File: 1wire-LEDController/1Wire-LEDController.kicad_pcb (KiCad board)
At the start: 2 copper layers, 99.8 x 99.8 mm, 33 parts, among them CON1 BARREL_JACK, J1 RJ45, J2 RJ45, P1 SWD, P2 Power Enable, P3 CONN_01X05, P4 DC_IN, P5 CONN_01X05, P6 UART, Q1 IRLZ44NS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

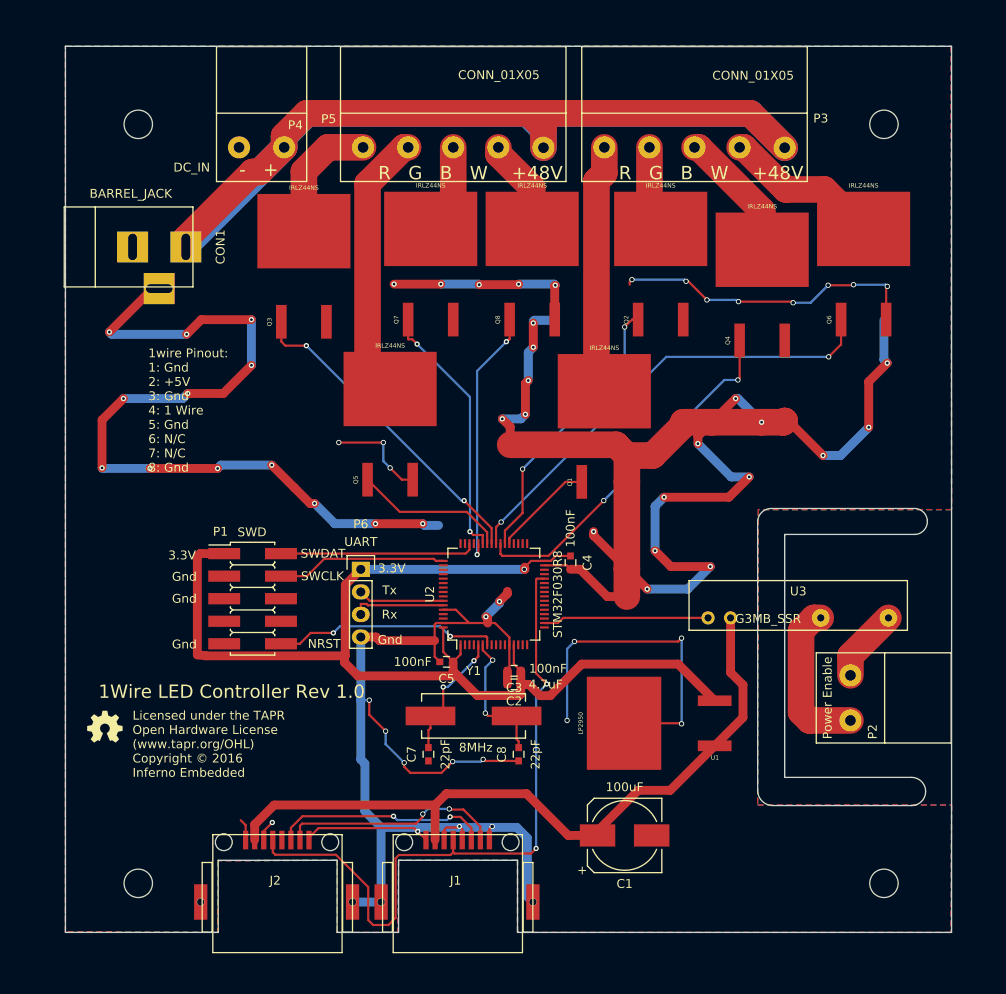
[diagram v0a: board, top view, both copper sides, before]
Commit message: Add 4 channel RGBW LED controller
Signed-off-by: Alastair D'Silva <alastair@d-silva.org>
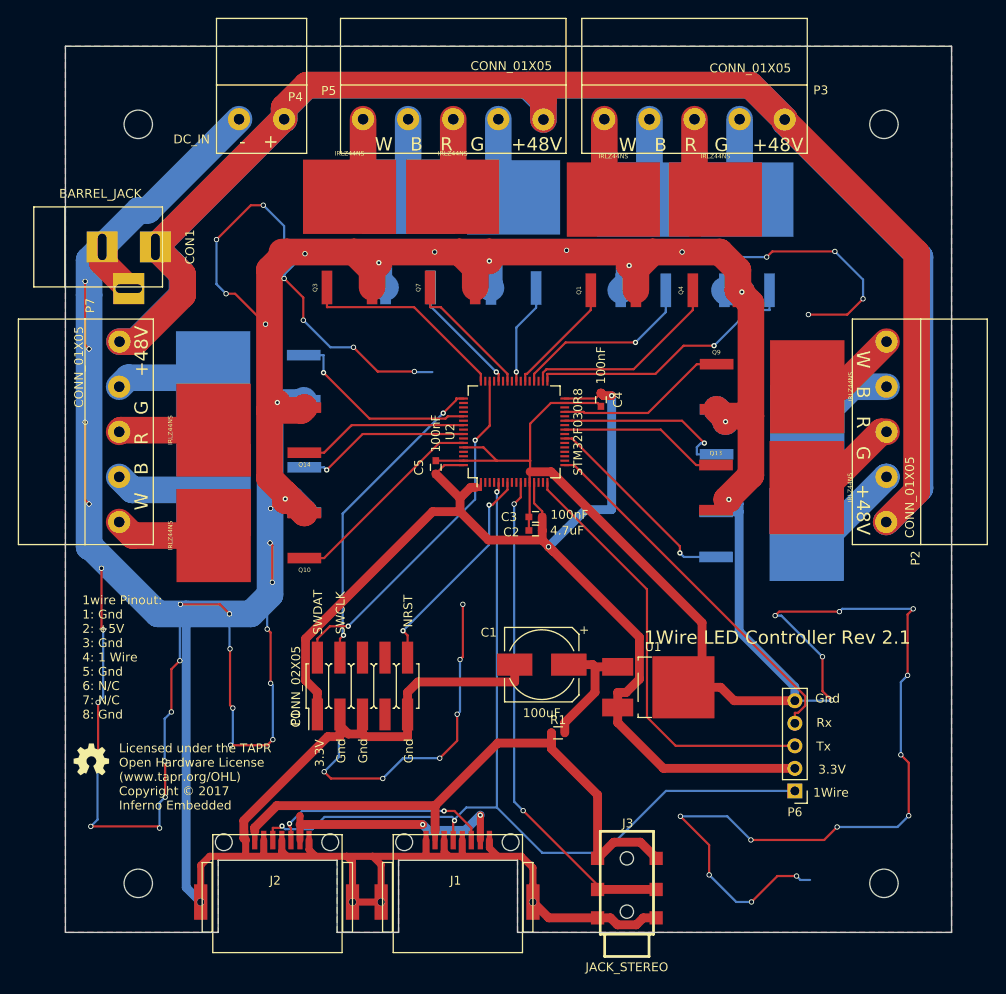
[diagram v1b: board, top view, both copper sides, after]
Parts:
- removed C7, C8: 22pF, Capacitors_SMD:C_0603
- removed U3: G3MB_SSR, SSR:G3MB
- removed Y1: 8MHz, Crystals:Crystal_HC49-SD_SMD
- added J3: JACK_STEREO, w_conn_av:jack_3.5_pj313d-smt, F.Cu at (193.0, 154.9)
- added P7: CONN_01X05, 2EDCK-Screw-Connectors:2EDCK-5.08-5PIN, F.Cu at (139.7, 116.8)
- added Q10: IRLZ44NS, kicad-open-modules:D2PAK, F.Cu at (146.5, 115.8)
- added Q11: IRLZ44NS, kicad-open-modules:D2PAK, B.Cu at (213.4, 104.1)
- added Q12: IRLZ44NS, kicad-open-modules:D2PAK, B.Cu at (146.5, 110.7)
- added Q13: IRLZ44NS, kicad-open-modules:D2PAK, F.Cu at (213.3, 110.4)
- added Q14: IRLZ44NS, kicad-open-modules:D2PAK, F.Cu at (146.5, 104.0)
- added Q15: IRLZ44NS, kicad-open-modules:D2PAK, B.Cu at (213.3, 115.7)
- added Q16: IRLZ44NS, kicad-open-modules:D2PAK, B.Cu at (146.4, 98.0)
- added Q9: IRLZ44NS, kicad-open-modules:D2PAK, F.Cu at (213.4, 99.1)
- added R1: 33R, Resistors_SMD:R_0603, F.Cu at (185.3, 138.0)
- P1: value SWD -> CONN_02X05
- P2: value Power Enable -> CONN_01X05; footprint 2EDCK-Screw-Connectors:2EDCK-5.08-2PIN -> 2EDCK-Screw-Connectors:2EDCK-5.08-5PIN
- P6: value UART -> CONN_01X05; footprint Pin_Headers:Pin_Header_Straight_1x04 -> Pin_Headers:Pin_Header_Straight_1x05_Pitch2.54mm
- Q2, Q5, Q6, Q8: moved to B.Cu
- U1: footprint kicad-open-modules:D2PAK -> TO_SOT_Packages_SMD:TO-252-2Lead
- moved P6 54.9 mm to (212.0, 144.6), turned to 180 degrees
- moved P2 37.8 mm to (218.4, 91.4)
- moved C5 21.9 mm to (171.5, 108.1), turned to 90 degrees
- moved Q5 21.7 mm to (168.4, 77.7), turned to 180 degrees
- moved Q1 21.6 mm to (191.5, 78.0)
- moved C1 21.4 mm to (183.5, 130.4), turned to 180 degrees
- moved C4 18.7 mm to (190.1, 100.5)
- moved U2 18.4 mm to (180.3, 104.1)
- moved C2 17.5 mm to (182.8, 115.3)
- moved C3 17.5 mm to (182.8, 113.7)
- moved P1 15.8 mm to (163.3, 132.8), turned to 0 degrees
- moved Q6 13.6 mm to (206.6, 78.0), turned to 180 degrees
- moved Q4 7.73 mm to (203.0, 78.0)
- moved Q3 6.44 mm to (161.8, 77.7)
- moved U1 5.04 mm to (195.7, 132.9), turned to 0 degrees
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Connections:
- net /PWM_Driver/SWCLK renamed /SWCLK
- net /PWM_Driver/SWDAT renamed /SWDAT
- C1 pad 1: +5V -> Net-(C1-Pad1)
- P6 pad 1: +3V3 -> /1W-DATA
- P6 pad 2: Net-(P6-Pad2) -> +3V3
- P6 pad 3: Net-(P6-Pad3) -> /UART_TX
- P6 pad 4: GND -> /UART_RX
- Q1 pad 1: Net-(Q1-Pad1) -> /CHAN2_R
- Q2 pad 1: Net-(Q2-Pad1) -> /CHAN2_G
- Q3 pad 1: Net-(Q3-Pad1) -> /CHAN1_R
- Q4 pad 1: Net-(Q4-Pad1) -> /CHAN2_B
- Q5 pad 1: Net-(Q5-Pad1) -> /CHAN1_G
- Q6 pad 1: Net-(Q6-Pad1) -> /CHAN2_W
- Q7 pad 1: Net-(Q7-Pad1) -> /CHAN1_B
- Q8 pad 1: Net-(Q8-Pad1) -> /CHAN1_W
- U1 pad 1: +5V -> Net-(C1-Pad1)
- U2 pad 10: (no net) -> /MAINS_ENABLE
- U2 pad 16: (no net) -> /UART_TX
- U2 pad 17: (no net) -> /UART_RX
- U2 pad 18: Net-(U2-Pad18) -> (no net)
- U2 pad 23: (no net) -> /CHAN3_W
- U2 pad 25: (no net) -> /CHAN3_B
- U2 pad 27: (no net) -> /CHAN3_G
- U2 pad 28: /1W-DATA -> (no net)
- U2 pad 29: (no net) -> /CHAN3_R
- U2 pad 33: (no net) -> /CHAN2_W
- U2 pad 34: (no net) -> /CHAN2_B
- U2 pad 36: (no net) -> /CHAN2_G
- U2 pad 37: Net-(Q1-Pad1) -> (no net)
- U2 pad 38: Net-(Q2-Pad1) -> /CHAN2_R
- U2 pad 39: Net-(Q4-Pad1) -> (no net)
- U2 pad 40: Net-(Q6-Pad1) -> /CHAN1_W
- U2 pad 41: Net-(Q3-Pad1) -> (no net)
- U2 pad 42: Net-(Q5-Pad1) -> /CHAN1_B
- U2 pad 43: Net-(Q7-Pad1) -> (no net)
- U2 pad 44: Net-(Q8-Pad1) -> /CHAN1_G
- U2 pad 48: (no net) -> /CHAN1_R
- U2 pad 5: Net-(C7-Pad2) -> /1W-DATA
- U2 pad 53: (no net) -> /CHAN0_W
- U2 pad 55: (no net) -> /CHAN0_B
- U2 pad 57: (no net) -> /CHAN0_G
- U2 pad 58: Net-(P6-Pad2) -> (no net)
- U2 pad 59: Net-(P6-Pad3) -> /CHAN0_R
- U2 pad 6: Net-(C8-Pad2) -> (no net)
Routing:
- net GND: track 518.5 -> 955.9 mm, vias 61 -> 63
- net +48V: track 161.5 -> 308.6 mm
- net /MAINS_ENABLE: track 0.00 -> 56.7 mm, vias 0 -> 2
- net Net-(Q6-Pad1): track 52.0 -> 0.00 mm, vias 2 -> 0
- net /UART_TX: track 0.00 -> 49.1 mm
- net /UART_RX: track 0.00 -> 41.6 mm
- net Net-(Q4-Pad1): track 40.7 -> 0.00 mm, vias 2 -> 0
- net (no net): track 0.00 -> 39.7 mm, vias 0 -> 6
- net Net-(Q3-Pad1): track 36.4 -> 0.00 mm, vias 2 -> 0
- net Net-(Q2-Pad1): track 31.9 -> 0.00 mm, vias 2 -> 0
- net /CHAN2_W: track 0.00 -> 31.0 mm, vias 0 -> 1
- net Net-(Q7-Pad1): track 29.6 -> 0.00 mm, vias 2 -> 0
- net Net-(Q8-Pad1): track 29.4 -> 0.00 mm, vias 2 -> 0
- net /1W-DATA: track 77.9 -> 105.7 mm, vias 2 -> 3
- net Net-(P5-Pad2): track 34.1 -> 8.74 mm
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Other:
- outline, holes or cut-outs redrawn
- board text added: "1Wire"
- board text added: "1Wire LED Controller Rev 2.1"
- board text added: "Licensed under the TAPR Open Hardware License (www.tapr.org/OHL) Copyright © 2017 Inferno Embedded"
- board text added: "W B R G"
- board text removed: "1Wire LED Controller Rev 1.0"
- board text removed: "Licensed under the TAPR Open Hardware License (www.tapr.org/OHL) Copyright © 2016 Inferno Embedded"
- board text removed: "R G B W"
